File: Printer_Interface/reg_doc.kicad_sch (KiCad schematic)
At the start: 0 parts

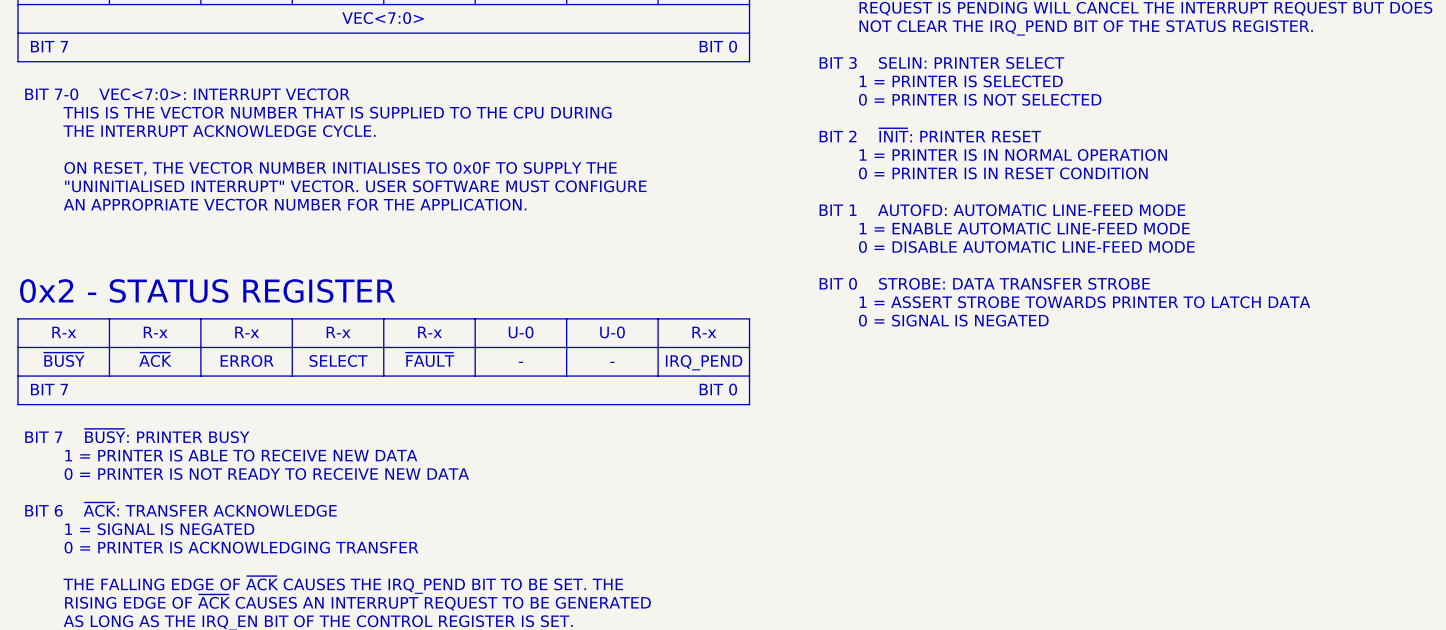
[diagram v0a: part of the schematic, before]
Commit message: Minor wording changes in register documentation
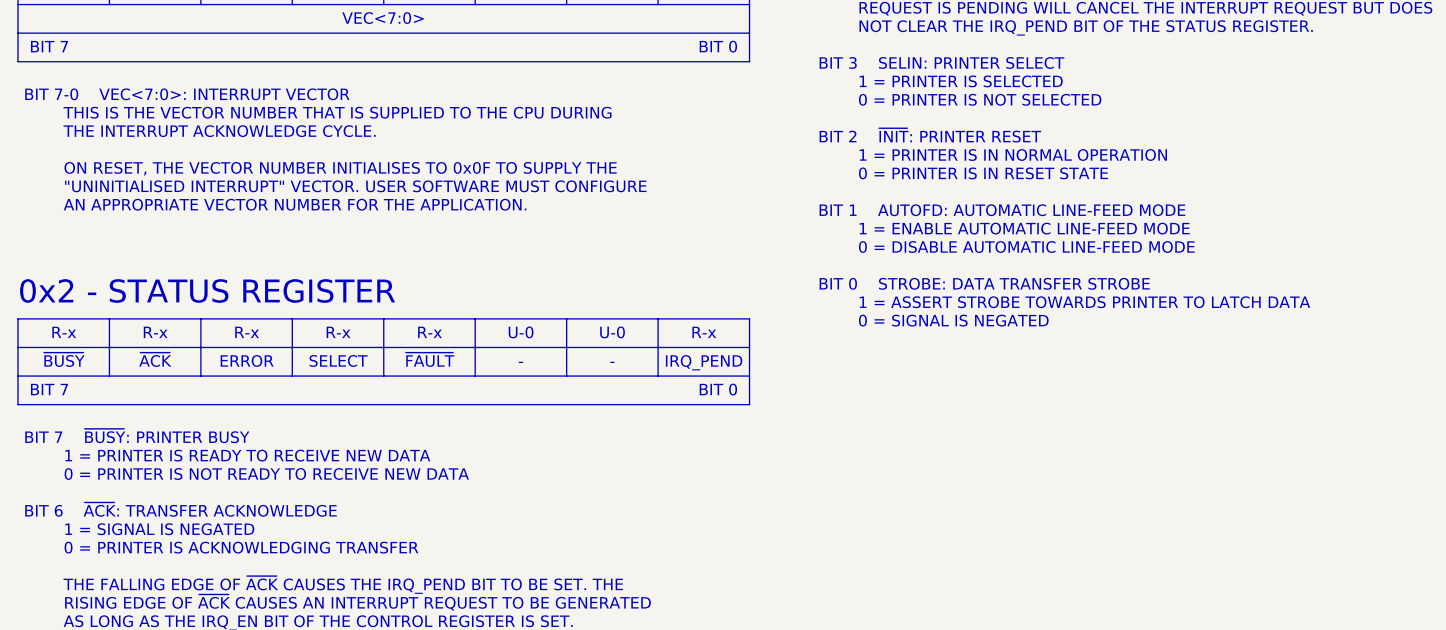
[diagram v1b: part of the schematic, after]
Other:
- note added: "BIT 7 ~{BUSY}: PRINTER BUSY 1 = PRINTER IS READY TO RECEIVE NEW DATA 0 = PRINTER IS NOT READY TO RECEIVE NEW DATA BIT 6 ~{ACK}: TRANSFER ACKNOWLEDGE 1 = SIGNAL IS NEGATED 0 = PRINTER IS ACKNOWLEDGING TRANSFER THE FALLING EDGE OF ~{ACK} CAUSES THE IRQ_PEND BIT TO BE SET. THE RISING EDGE OF ~{ACK} CAUSES AN INTERRUPT REQUEST TO BE GENERATED AS LONG AS THE IRQ_EN BIT OF THE CONTROL REGISTER IS SET. 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"
- note removed: "BIT 7 ~{BUSY}: PRINTER BUSY 1 = PRINTER IS ABLE TO RECEIVE NEW DATA 0 = PRINTER IS NOT READY TO RECEIVE NEW DATA BIT 6 ~{ACK}: TRANSFER ACKNOWLEDGE 1 = SIGNAL IS NEGATED 0 = PRINTER IS ACKNOWLEDGING TRANSFER THE FALLING EDGE OF ~{ACK} CAUSES THE IRQ_PEND BIT TO BE SET. THE RISING EDGE OF ~{ACK} CAUSES AN INTERRUPT REQUEST TO BE GENERATED AS LONG AS THE IRQ_EN BIT OF THE CONTROL REGISTER IS SET. B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"
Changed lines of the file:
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@@
 		)
 	)
-	(text "BIT 7	IN_USE: IN USE LED CONTROL\n		1 = LED ON\n		0 = LED OFF\n\nBIT 6-5	UNIMPLEMENTED\n\nBIT 4	IRQ_EN: INTERRUPT REQUEST ENABLE\n		1 = INTERRUPT WILL BE GENERATED ON THE RISING EDGE OF ~{ACK}\n		0 = INTERRUPTS ARE DISABLED\n\n		WHEN IRQ_EN IS CLEARED, INTERRUPT REQUESTS ARE INHIBITED BUT THE\n		IRQ_PEND BIT OF THE STATUS REGISTER WILL STILL REFLECT PENDING\n		INTERRUPT CONDITIONS. CLEARING IRQ_EN WHILE AN INTERRUPT\n		REQUEST IS PENDING WILL CANCEL THE INTERRUPT REQUEST BUT DOES\n		NOT CLEAR THE IRQ_PEND BIT OF THE STATUS REGISTER.\n\nBIT 3	SELIN: PRINTER SELECT\n		1 = PRINTER IS SELECTED\n		0 = PRINTER IS NOT SELECTED\n\nBIT 2	~{INIT}: PRINTER RESET\n		1 = PRINTER IS IN NORMAL OPERATION\n		0 = PRINTER IS IN RESET CONDITION\n\nBIT 1	AUTOFD: AUTOMATIC LINE-FEED MODE\n		1 = ENABLE AUTOMATIC LINE-FEED MODE\n		0 = DISABLE AUTOMATIC LINE-FEED MODE\n\nBIT 0	STROBE: DATA TRANSFER STROBE\n		1 = ASSERT STROBE TOWARDS PRINTER TO LATCH DATA\n		0 = SIGNAL IS NEGATED"
+	(text "BIT 7	IN_USE: IN USE LED CONTROL\n		1 = LED ON\n		0 = LED OFF\n\nBIT 6-5	UNIMPLEMENTED\n\nBIT 4	IRQ_EN: INTERRUPT REQUEST ENABLE\n		1 = INTERRUPT WILL BE GENERATED ON THE RISING EDGE OF ~{ACK}\n		0 = INTERRUPTS ARE DISABLED\n\n		WHEN IRQ_EN IS CLEARED, INTERRUPT REQUESTS ARE INHIBITED BUT THE\n		IRQ_PEND BIT OF THE STATUS REGISTER WILL STILL REFLECT PENDING\n		INTERRUPT CONDITIONS. CLEARING IRQ_EN WHILE AN INTERRUPT\n		REQUEST IS PENDING WILL CANCEL THE INTERRUPT REQUEST BUT DOES\n		NOT CLEAR THE IRQ_PEND BIT OF THE STATUS REGISTER.\n\nBIT 3	SELIN: PRINTER SELECT\n		1 = PRINTER IS SELECTED\n		0 = PRINTER IS NOT SELECTED\n\nBIT 2	~{INIT}: PRINTER RESET\n		1 = PRINTER IS IN NORMAL OPERATION\n		0 = PRINTER IS IN RESET STATE\n\nBIT 1	AUTOFD: AUTOMATIC LINE-FEED MODE\n		1 = ENABLE AUTOMATIC LINE-FEED MODE\n		0 = DISABLE AUTOMATIC LINE-FEED MODE\n\nBIT 0	STROBE: DATA TRANSFER STROBE\n		1 = ASSERT STROBE TOWARDS PRINTER TO LATCH DATA\n		0 = SIGNAL IS NEGATED"
 		(exclude_from_sim no)
 		(at 109.22 36.83 0)
@@
 		)
 	)
-	(text "BIT 7	~{BUSY}: PRINTER BUSY\n		1 = PRINTER IS ABLE TO RECEIVE NEW DATA\n		0 = PRINTER IS NOT READY TO RECEIVE NEW DATA\n\nBIT 6	~{ACK}: TRANSFER ACKNOWLEDGE\n		1 = SIGNAL IS NEGATED\n		0 = PRINTER IS ACKNOWLEDGING TRANSFER\n\n		THE FALLING EDGE OF ~{ACK} CAUSES THE IRQ_PEND BIT TO BE SET. THE\n		RISING EDGE OF ~{ACK} CAUSES AN INTERRUPT REQUEST TO BE GENERATED\n		AS LONG AS THE IRQ_EN BIT OF THE CONTROL REGISTER IS SET.\n\nBIT 5	ERROR: PAPER ERROR\n		1 = PRINTER IS EXPERIENCING AN ERROR IN THE PAPER PATH\n		0 = NO ERROR CONDITION EXISTS\n\nBIT 4	SELECT: PRINTER ONLINE INDICATOR\n		1 = PRINTER IS ONLINE\n		0 = PRINTER IS NOT ONLINE\n\nBIT 3	~{FAULT}: PRINTER FAULT INDICATOR\n		1 = NO FAULT CONDITION EXISTS\n		0 = PRINTER IS EXPERIENCING A FAULT\n\nBIT 2-1	UNIMPLEMENTED\n\nBIT 0	IRQ_PEND: INTERRUPT PENDING\n		1 = AN INTERRUPT IS CURRENTLY PENDING FOR THIS INTERFACE\n		0 = NO INTERRUPT PENDING\n\n		IRQ_PEND REMAINS SET AS LONG AS THE ~{ACK} SIGNAL IS ASSERTED, AND\n		IS CLEARED BY READING THE STATUS REGISTER ONCE ~{ACK} IS NEGATED."
+	(text "BIT 7	~{BUSY}: PRINTER BUSY\n		1 = PRINTER IS READY TO RECEIVE NEW DATA\n		0 = PRINTER IS NOT READY TO RECEIVE NEW DATA\n\nBIT 6	~{ACK}: TRANSFER ACKNOWLEDGE\n		1 = SIGNAL IS NEGATED\n		0 = PRINTER IS ACKNOWLEDGING TRANSFER\n\n		THE FALLING EDGE OF ~{ACK} CAUSES THE IRQ_PEND BIT TO BE SET. THE\n		RISING EDGE OF ~{ACK} CAUSES AN INTERRUPT REQUEST TO BE GENERATED\n		AS LONG AS THE IRQ_EN BIT OF THE CONTROL REGISTER IS SET.\n\nBIT 5	ERROR: PAPER ERROR\n		1 = PRINTER IS EXPERIENCING AN ERROR IN THE PAPER PATH\n		0 = NO ERROR CONDITION EXISTS\n\nBIT 4	SELECT: PRINTER ONLINE INDICATOR\n		1 = PRINTER IS ONLINE\n		0 = PRINTER IS NOT ONLINE\n\nBIT 3	~{FAULT}: PRINTER FAULT INDICATOR\n		1 = NO FAULT CONDITION EXISTS\n		0 = PRINTER IS EXPERIENCING A FAULT\n\nBIT 2-1	UNIMPLEMENTED\n\nBIT 0	IRQ_PEND: INTERRUPT PENDING\n		1 = AN INTERRUPT IS CURRENTLY PENDING FOR THIS INTERFACE\n		0 = NO INTERRUPT PENDING\n\n		IRQ_PEND REMAINS SET AS LONG AS THE ~{ACK} SIGNAL IS ASSERTED, AND\n		IS CLEARED BY READING THE STATUS REGISTER ONCE ~{ACK} IS NEGATED."
 		(exclude_from_sim no)
 		(at 20.955 111.125 0)

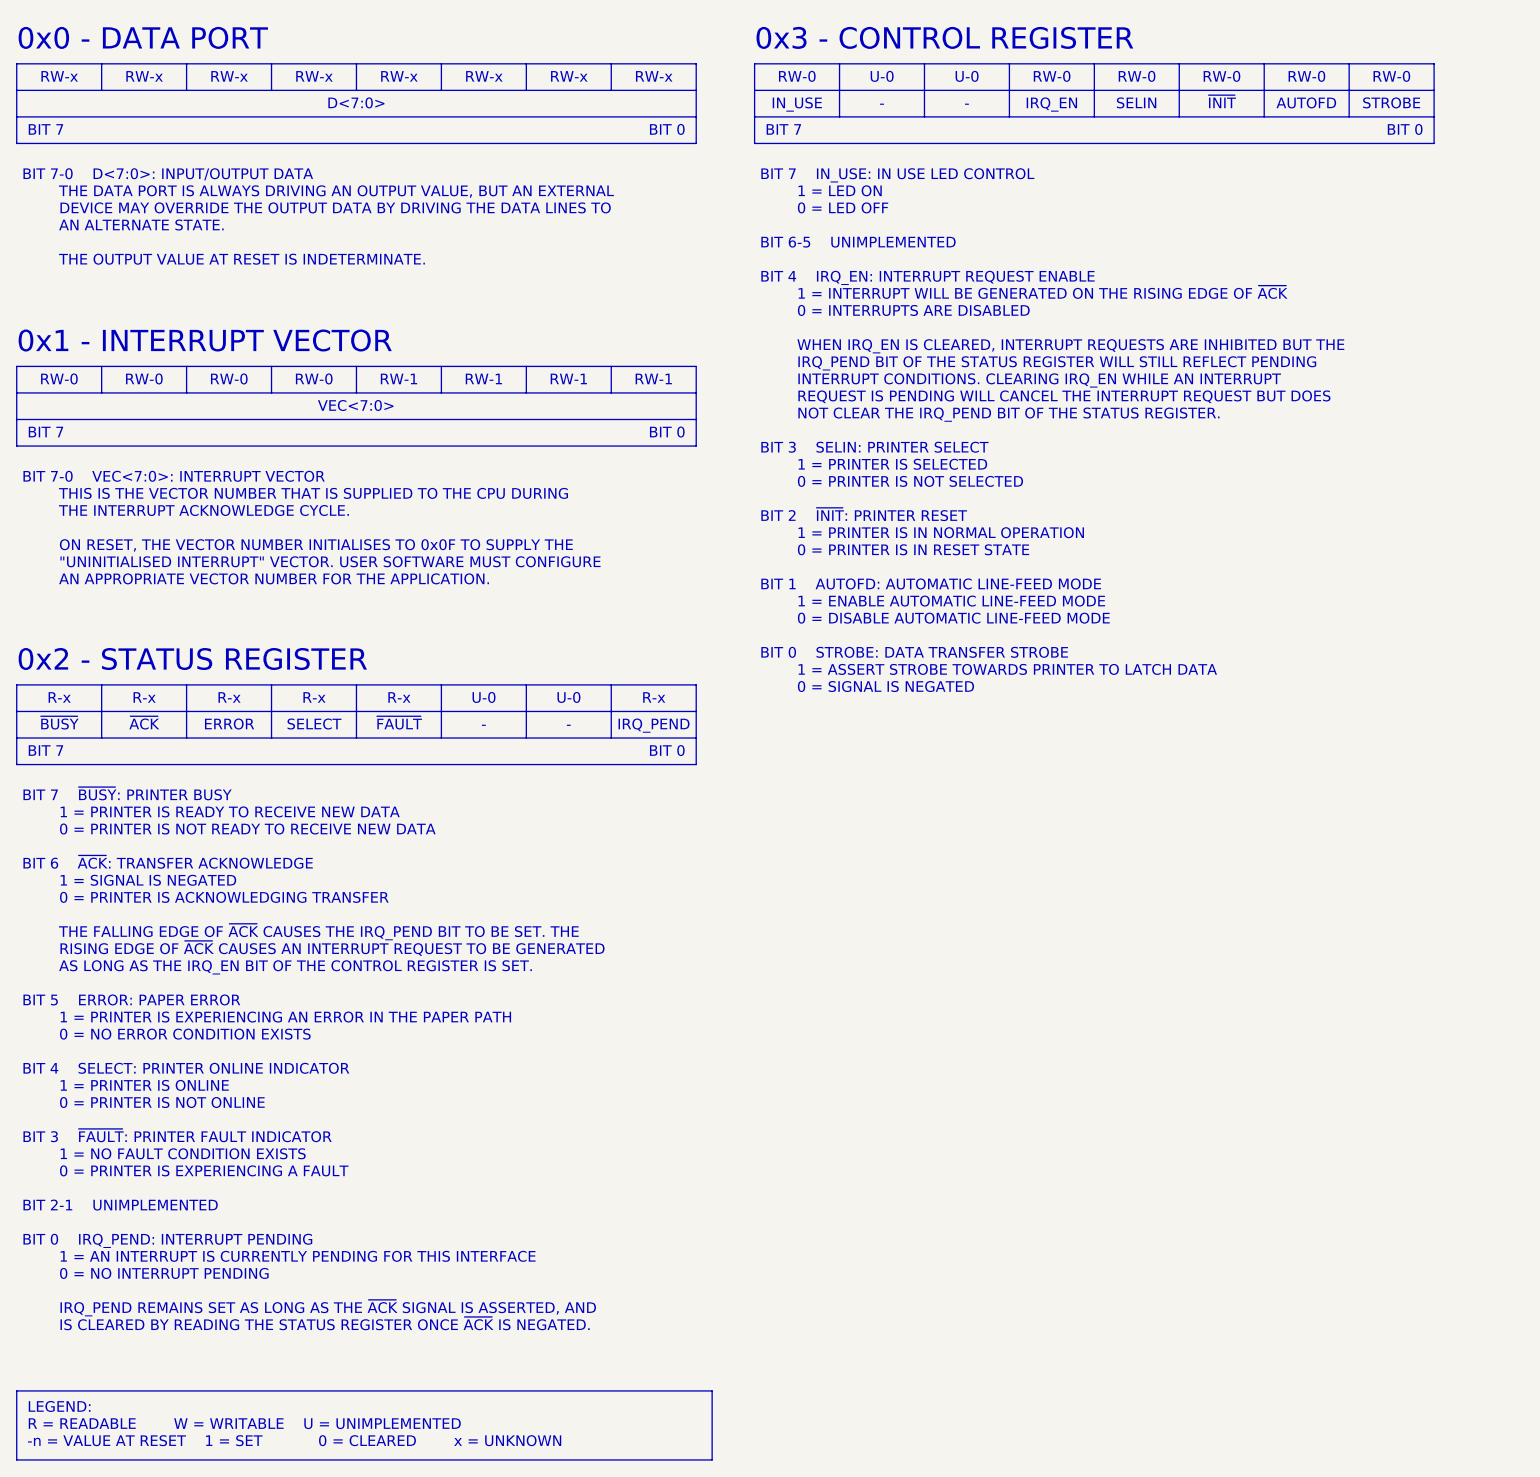
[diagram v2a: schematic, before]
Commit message: Some changes
* Consolidate some parts around the 74HCT373 latch
* Add memory map
* Update ibom
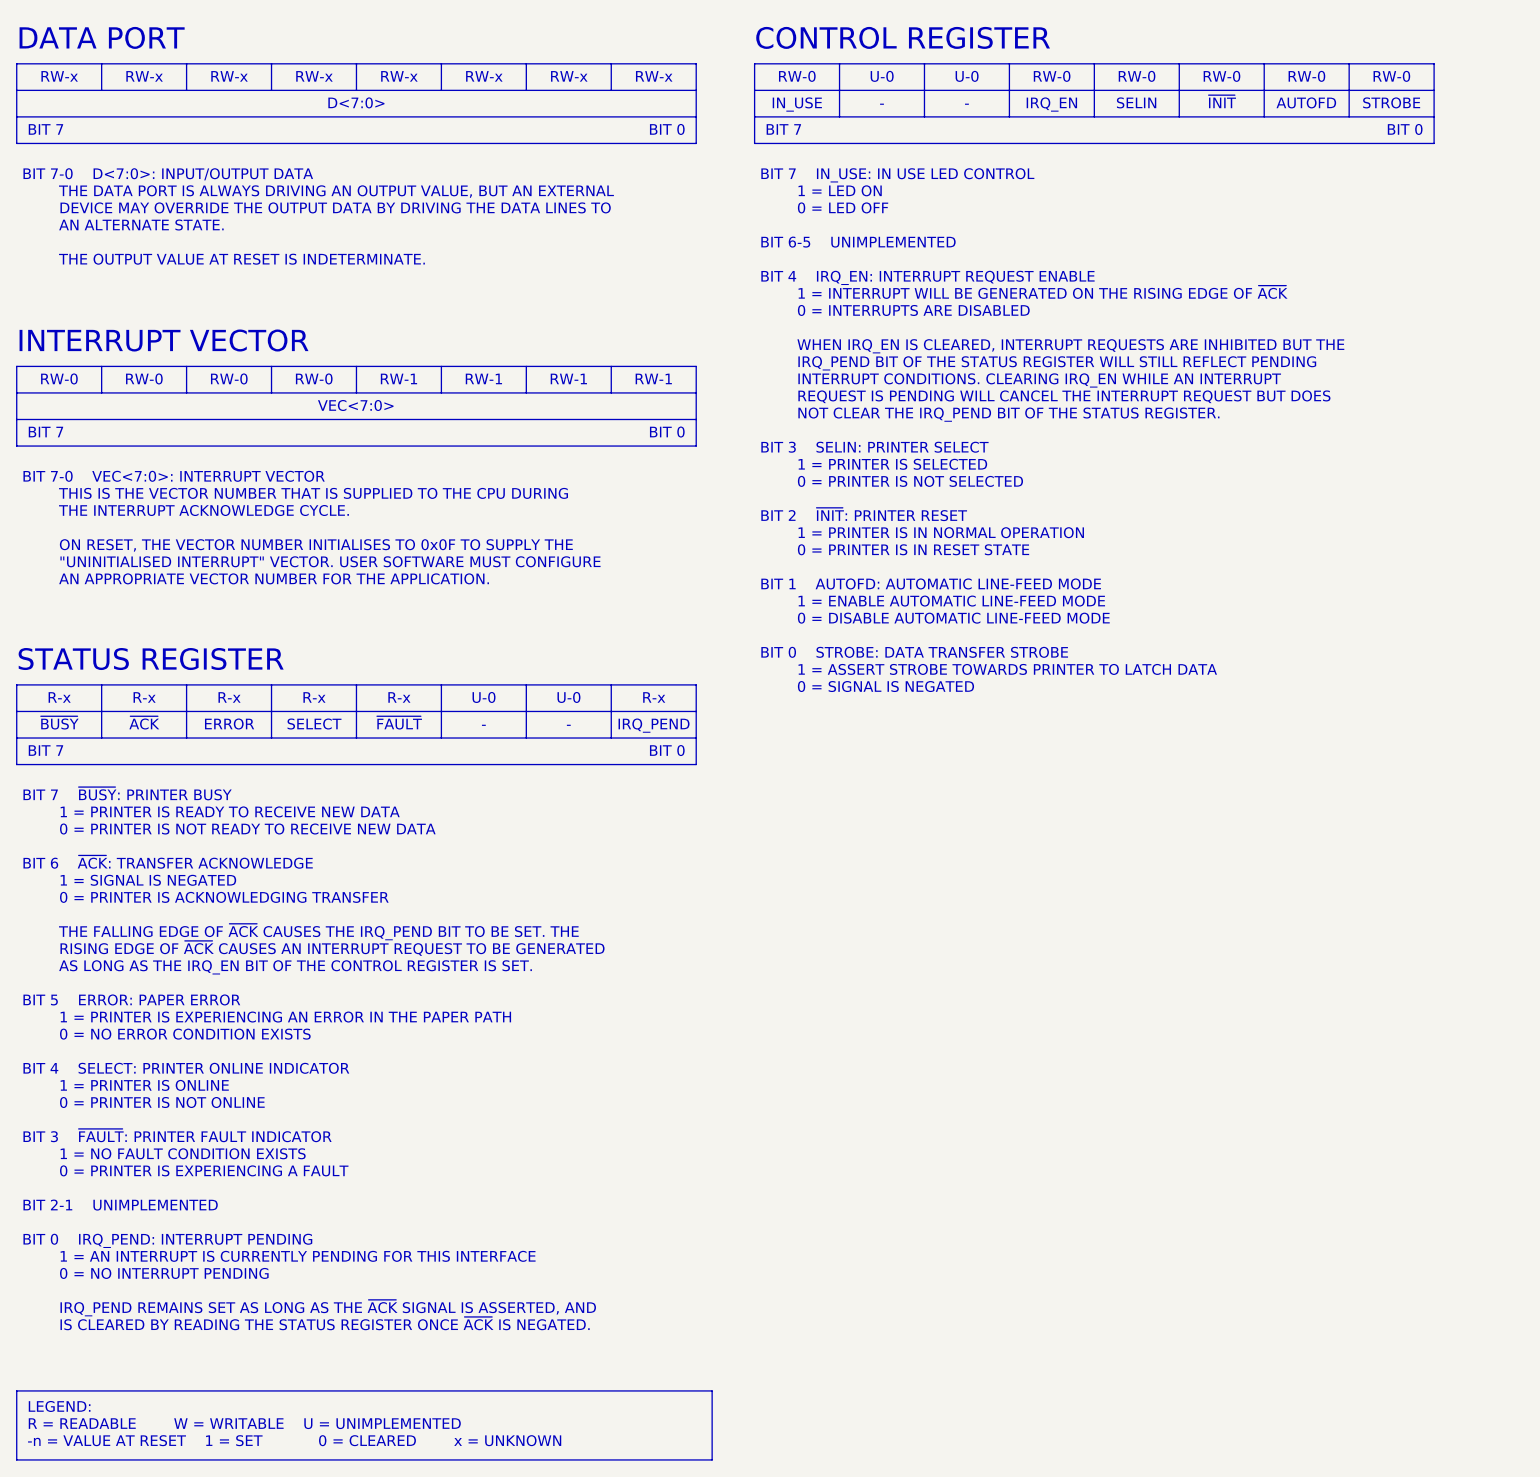
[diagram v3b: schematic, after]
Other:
- note added: "CONTROL REGISTER"
- note added: "DATA PORT"
- note added: "INTERRUPT VECTOR"
- note added: "STATUS REGISTER"
- note removed: "0x0 - DATA PORT"
- note removed: "0x1 - INTERRUPT VECTOR"
- note removed: "0x2 - STATUS REGISTER"
- note removed: "0x3 - CONTROL REGISTER"
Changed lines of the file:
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@@
 	(title_block
 		(title "REGISTER DOCUMENTATION")
-		(date "2024-03-12")
+		(date "2024-03-24")
 		(rev "1")
 		(company "(C) TOM STOREY")
@@
 		)
 	)
-	(text "0x0 - DATA PORT"
+	(text "DATA PORT"
 		(exclude_from_sim no)
 		(at 20.32 22.86 0)
@@
 		)
 	)
-	(text "0x2 - STATUS REGISTER"
+	(text "STATUS REGISTER"
 		(exclude_from_sim no)
 		(at 20.32 97.155 0)
@@
 		)
 	)
-	(text "0x3 - CONTROL REGISTER"
+	(text "CONTROL REGISTER"
 		(exclude_from_sim no)
 		(at 108.585 22.86 0)
@@
 		)
 	)
-	(text "0x1 - INTERRUPT VECTOR"
+	(text "INTERRUPT VECTOR"
 		(exclude_from_sim no)
 		(at 20.32 59.055 0)
